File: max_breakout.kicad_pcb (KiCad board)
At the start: 4 copper layers, 50.8 x 30 mm, 44 parts, among them J1 USB_B_Micro, J2 PMOD, J3 Left, J4 Right, J5 JTAG, SW1 User, U1 TXS0108EPW, U2 LP2985-3.3, U3 LP2985-5.0, U4 TPS2113A, U5 EPM7064STC44, X1 CTX-636 50mhz

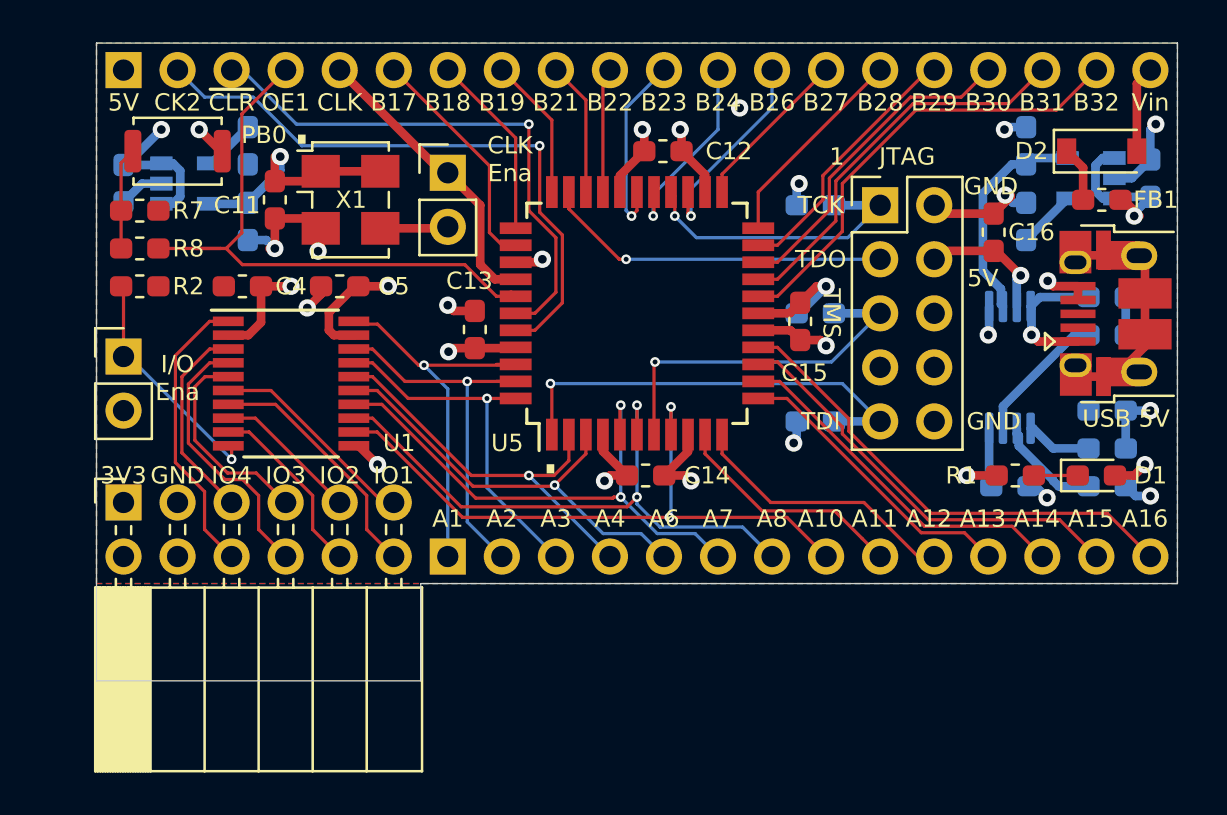
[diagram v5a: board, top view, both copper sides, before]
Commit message: added gnd and input pins
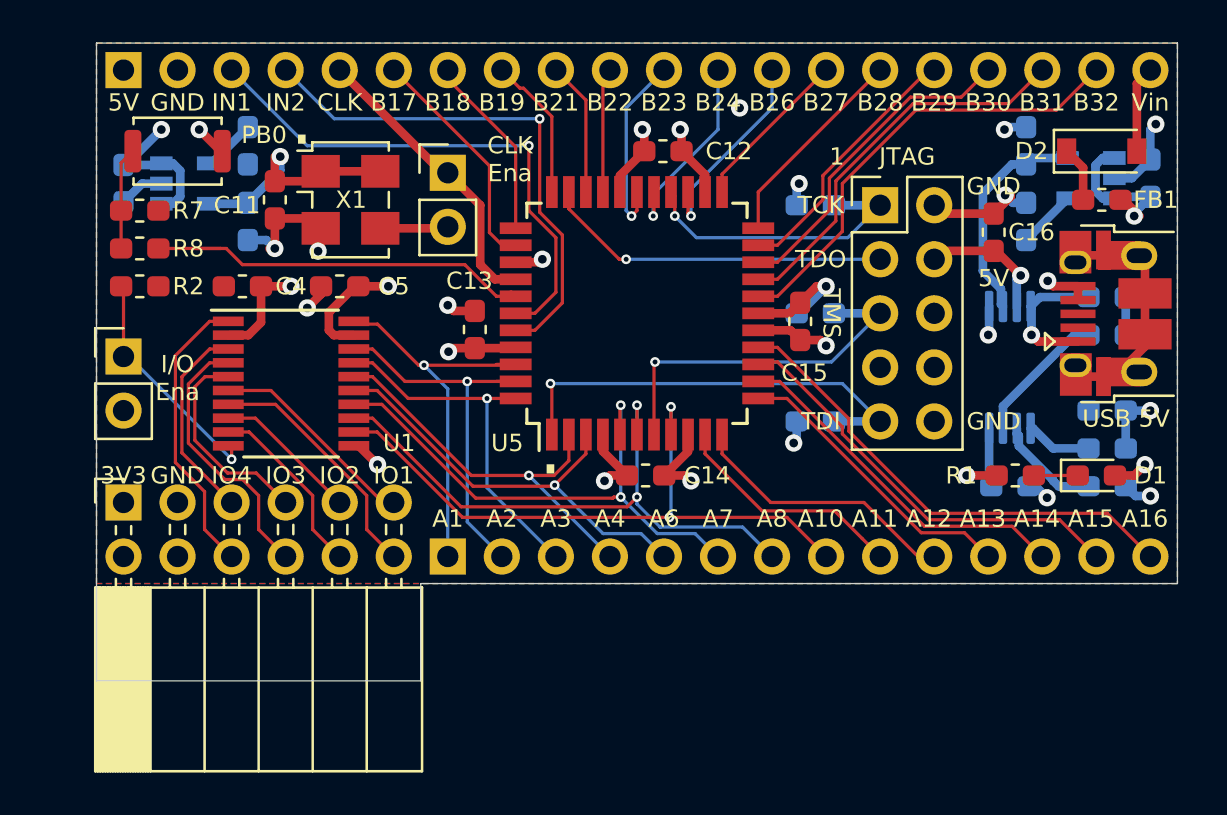
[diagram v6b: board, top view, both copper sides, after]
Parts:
- D1: value RED -> BLU
- R2: value 100K -> 10K
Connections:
- net /GCLRn renamed /IN1
- J4 pad 2: /CLK2 -> GND
- J4 pad 4: /OE1 -> /IN2
- R8 pad 1: /OE1 -> /PB0
- U5 pad 38: /OE1 -> /PB0
- U5 pad 40: /CLK2 -> /IN2
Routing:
- net /CLK2: track 29.8 -> 0.00 mm, vias 1 -> 0
- net /OE1: track 28.7 -> 0.00 mm
- net /IN2: track 0.00 -> 25.3 mm, vias 0 -> 1
- net /PB0: track 0.00 -> 19.2 mm
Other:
- board text added: "IN1"
- board text added: "IN2"
- board text removed: "CK2"
- board text removed: "OE1"
- board text removed: "~CLR"

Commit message: Silkscreen adjustments
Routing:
- net GND: vias 19 -> 21

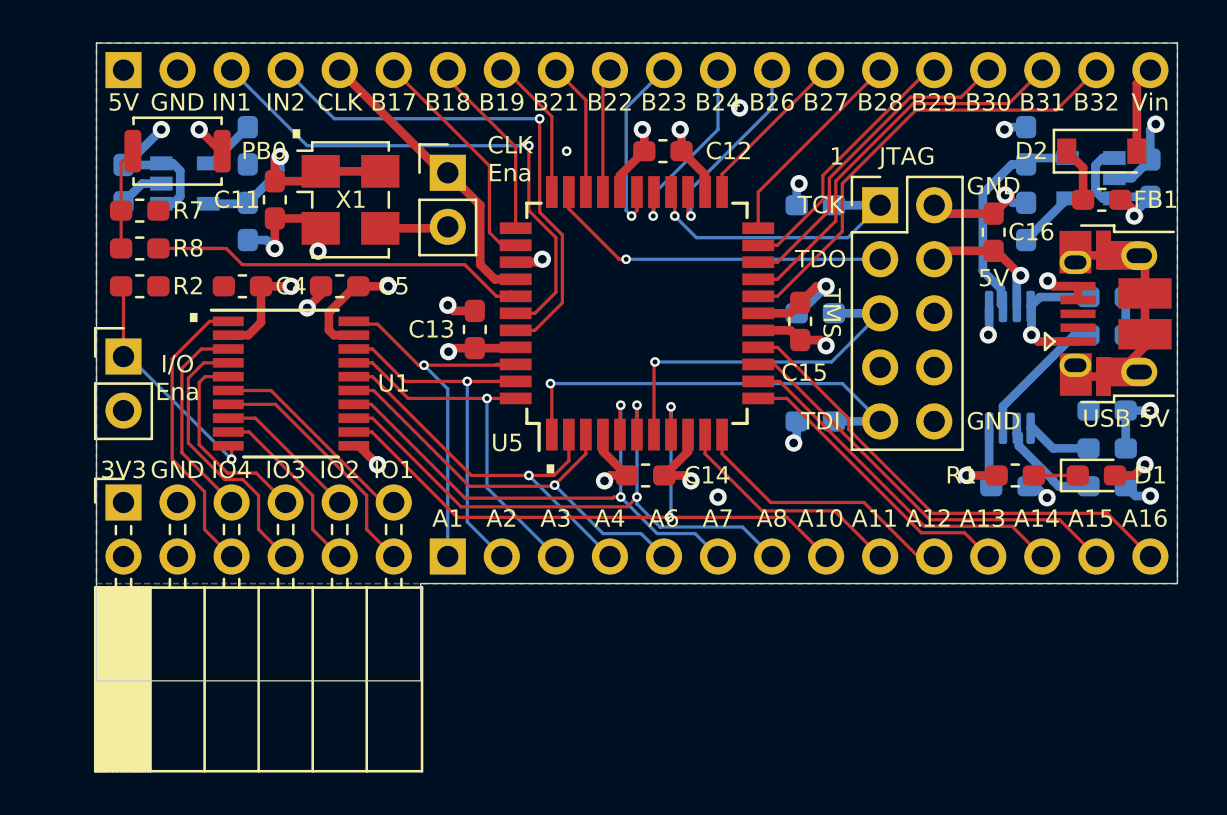
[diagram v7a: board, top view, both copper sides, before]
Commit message: flipped some components to front-side
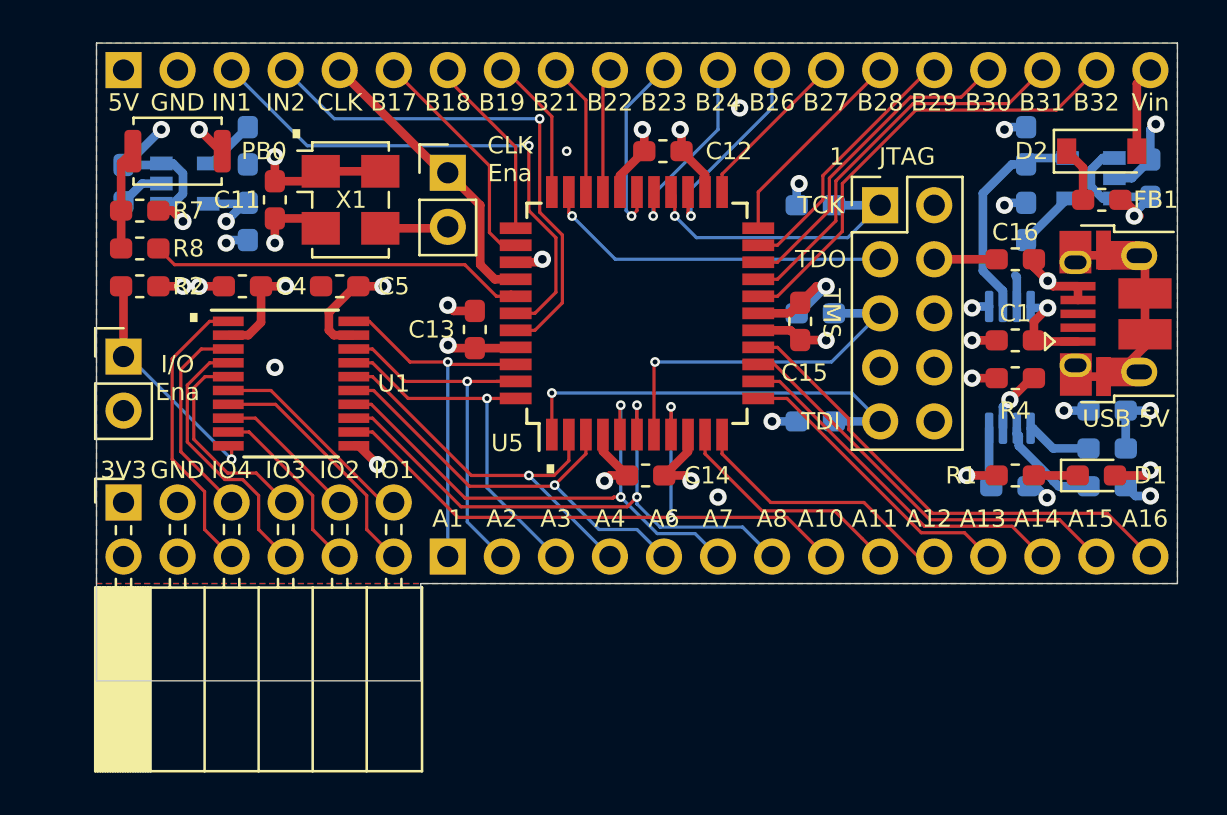
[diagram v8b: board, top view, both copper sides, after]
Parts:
- C1, R4: moved to F.Cu
- moved C1 4.77 mm to (167.6, 105.4), turned to 180 degrees
- moved R4 4.77 mm to (167.6, 107.2), turned to 180 degrees
- moved C16 1.63 mm to (167.6, 101.6), turned to 0 degrees
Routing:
- net Net-(R4-Pad1): track 6.44 -> 3.02 mm, vias 0 -> 1
- net +3V3: track 16.1 -> 14.4 mm, vias 2 -> 3
- net Net-(C1-Pad1): track 6.57 -> 5.03 mm
- net +5V: track 43.4 -> 42.2 mm, vias 11 -> 10
- net /A1: track 18.8 -> 17.6 mm
- net /PB0: track 19.2 -> 18.0 mm
- net /TDI: track 20.8 -> 20.1 mm
- net GND: track 45.6 -> 45.0 mm, vias 21 -> 27
